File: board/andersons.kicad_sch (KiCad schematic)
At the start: 13 parts, among them J10 768250002, J11 768250002, J12 768250002, J13 768250002, J14 768250002, J15 768250002, J16 768250002, J17 768250002, J18 768250002, J6 768250002, J7 768250002, J8 768250002, J9 768250002

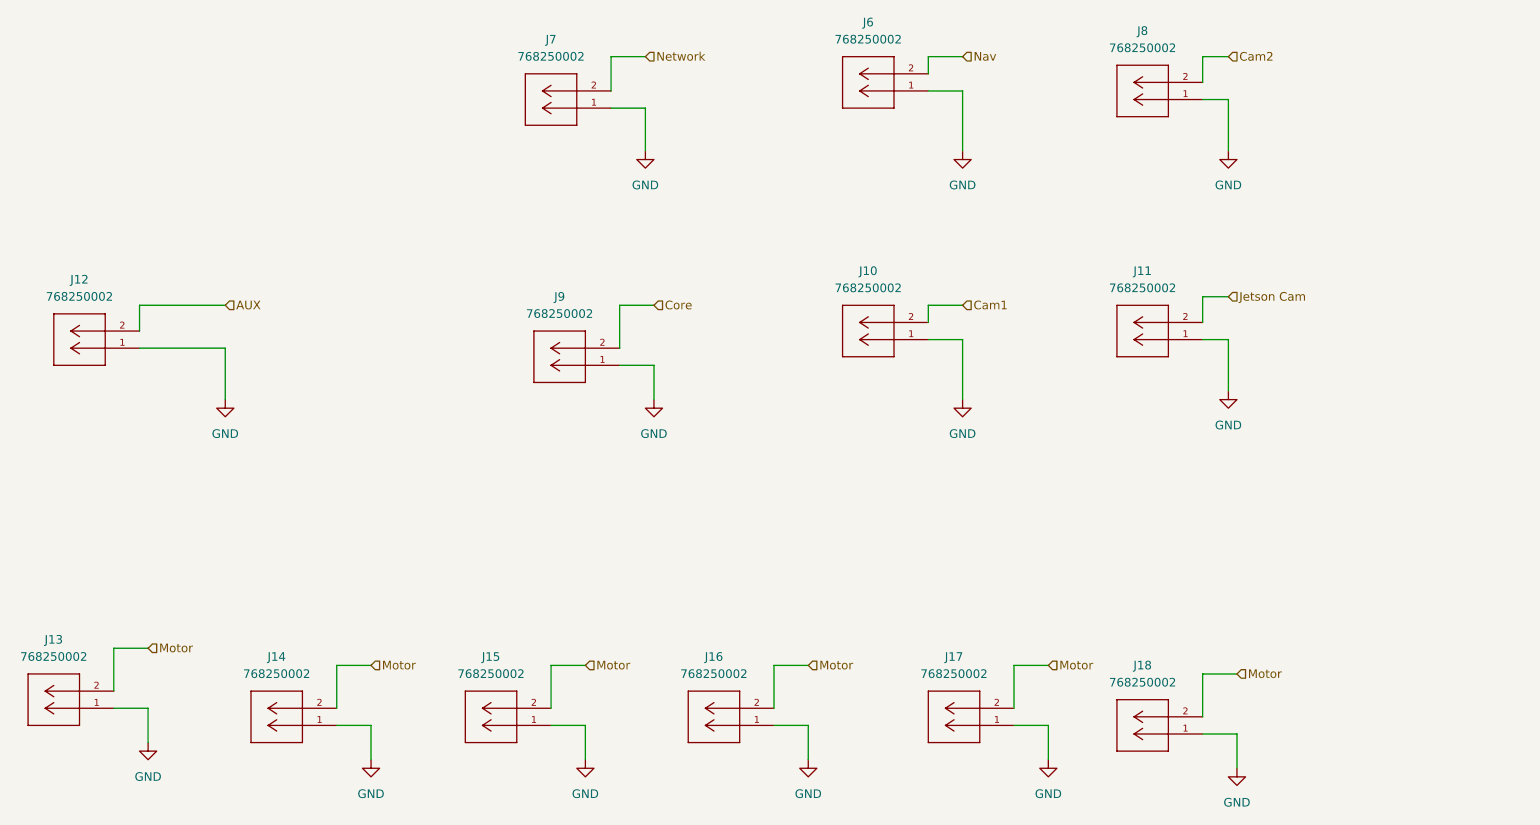
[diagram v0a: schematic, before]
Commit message: Center schematics and layout for prettiness
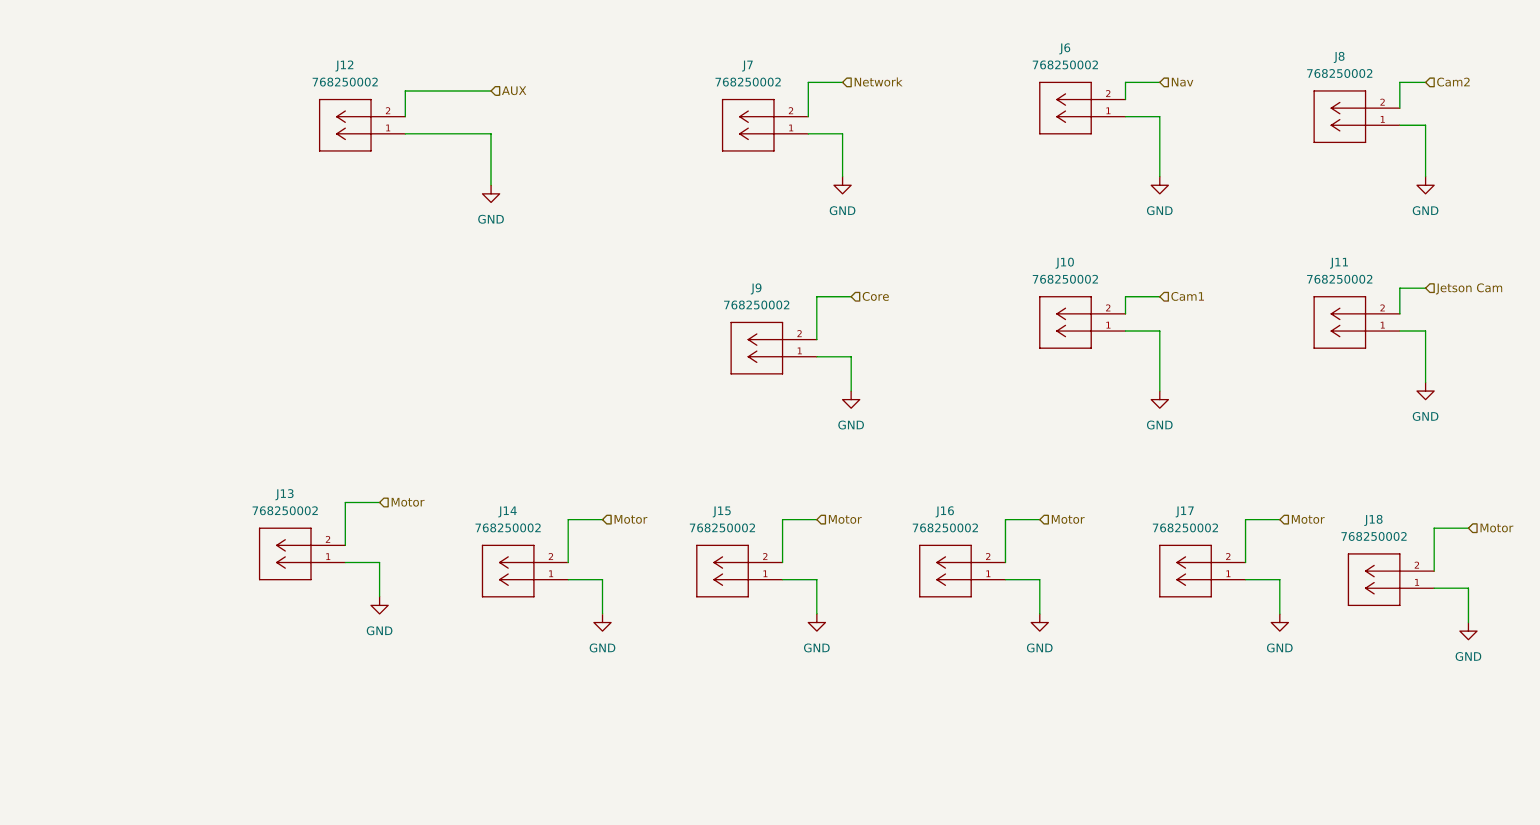
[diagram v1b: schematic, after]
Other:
- moved on the sheet: J10, J11, J12, J13, J14, J15, J16, J17, J18, J6, J7, J8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

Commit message: add label for battery sensing molex connector
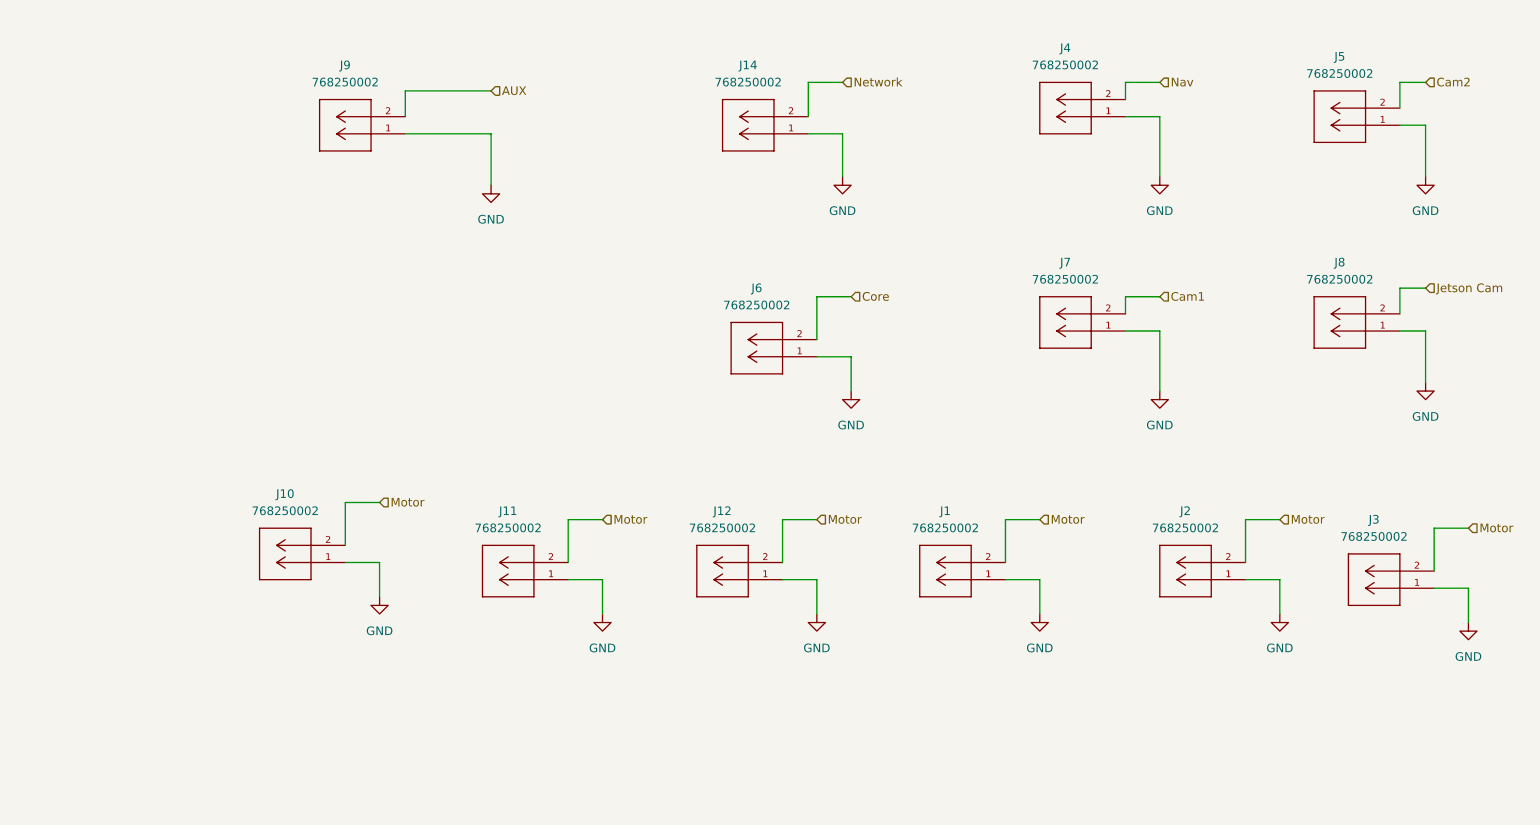
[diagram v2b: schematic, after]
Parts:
- renumbered J16 to J1, J13 to J10, J14 to J11, J15 to J12, J7 to J14, J17 to J2, J18 to J3, J6 to J4, J8 to J5, J9 to J6, J10 to J7, J11 to J8, J12 to J9
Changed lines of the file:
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@@
 		(dnp no)
 		(fields_autoplaced yes)
-		(property "Reference" "J6"
+		(property "Reference" "J4"
 			(at 176.53 39.37 0)
 			(effects
@@
 			(project ""
 				(path "/7eaa639d-7062-45e7-be05-1c2855431307/7df83f93-7851-4dc4-9a38-c4dfcc370e8d"
-					(reference "J6")
+					(reference "J4")
 					(unit 1)
 				)
@@
 		(dnp no)
 		(fields_autoplaced yes)
-		(property "Reference" "J18"
+		(property "Reference" "J3"
 			(at 222.25 109.22 0)
 			(effects
@@
 			(project "PowerManagementBoard"
 				(path "/7eaa639d-7062-45e7-be05-1c2855431307/7df83f93-7851-4dc4-9a38-c4dfcc370e8d"
-					(reference "J18")
+					(reference "J3")
 					(unit 1)
 				)
@@
 		(dnp no)
 		(fields_autoplaced yes)
-		(property "Reference" "J17"
+		(property "Reference" "J2"
 			(at 194.31 107.95 0)
 			(effects
@@
 			(project "PowerManagementBoard"
 				(path "/7eaa639d-7062-45e7-be05-1c2855431307/7df83f93-7851-4dc4-9a38-c4dfcc370e8d"
-					(reference "J17")
+					(reference "J2")
 					(unit 1)
 				)
@@
 		(dnp no)
 		(fields_autoplaced yes)
-		(property "Reference" "J7"
+		(property "Reference" "J14"
 			(at 129.54 41.91 0)
 			(effects
@@
 			(project "PowerManagementBoard"
 				(path "/7eaa639d-7062-45e7-be05-1c2855431307/7df83f93-7851-4dc4-9a38-c4dfcc370e8d"
-					(reference "J7")
+					(reference "J14")
 					(unit 1)
 				)
@@
 		(dnp no)
 		(fields_autoplaced yes)
-		(property "Reference" "J12"
+		(property "Reference" "J9"
 			(at 69.85 41.91 0)
 			(effects
@@
 			(project "PowerManagementBoard"
 				(path "/7eaa639d-7062-45e7-be05-1c2855431307/7df83f93-7851-4dc4-9a38-c4dfcc370e8d"
-					(reference "J12")
+					(reference "J9")
 					(unit 1)
 				)
@@
 		(dnp no)
 		(fields_autoplaced yes)
-		(property "Reference" "J9"
+		(property "Reference" "J6"
 			(at 130.81 74.93 0)
 			(effects
@@
 			(project "PowerManagementBoard"
 				(path "/7eaa639d-7062-45e7-be05-1c2855431307/7df83f93-7851-4dc4-9a38-c4dfcc370e8d"
-					(reference "J9")
+					(reference "J6")
 					(unit 1)
 				)
@@
 		(dnp no)
 		(fields_autoplaced yes)
-		(property "Reference" "J16"
+		(property "Reference" "J1"
 			(at 158.75 107.95 0)
 			(effects
@@
 			(project "PowerManagementBoard"
 				(path "/7eaa639d-7062-45e7-be05-1c2855431307/7df83f93-7851-4dc4-9a38-c4dfcc370e8d"
-					(reference "J16")
+					(reference "J1")
 					(unit 1)
 				)
@@
 		(dnp no)
 		(fields_autoplaced yes)
-		(property "Reference" "J8"
+		(property "Reference" "J5"
 			(at 217.17 40.64 0)
 			(effects
@@
 			(project "PowerManagementBoard"
 				(path "/7eaa639d-7062-45e7-be05-1c2855431307/7df83f93-7851-4dc4-9a38-c4dfcc370e8d"
-					(reference "J8")
+					(reference "J5")
 					(unit 1)
 				)
@@
 		(dnp no)
 		(fields_autoplaced yes)
-		(property "Reference" "J14"
+		(property "Reference" "J11"
 			(at 93.98 107.95 0)
 			(effects
@@
 			(project "PowerManagementBoard"
 				(path "/7eaa639d-7062-45e7-be05-1c2855431307/7df83f93-7851-4dc4-9a38-c4dfcc370e8d"
-					(reference "J14")
+					(reference "J11")
 					(unit 1)
 				)
@@
 		(dnp no)
 		(fields_autoplaced yes)
-		(property "Reference" "J10"
+		(property "Reference" "J7"
 			(at 176.53 71.12 0)
 			(effects
@@
 			(project "PowerManagementBoard"
 				(path "/7eaa639d-7062-45e7-be05-1c2855431307/7df83f93-7851-4dc4-9a38-c4dfcc370e8d"
-					(reference "J10")
+					(reference "J7")
 					(unit 1)
 				)
@@
 		(dnp no)
 		(fields_autoplaced yes)
-		(property "Reference" "J11"
+		(property "Reference" "J8"
 			(at 217.17 71.12 0)
 			(effects
@@
 			(project "PowerManagementBoard"
 				(path "/7eaa639d-7062-45e7-be05-1c2855431307/7df83f93-7851-4dc4-9a38-c4dfcc370e8d"
-					(reference "J11")
+					(reference "J8")
 					(unit 1)
 				)
@@
 		(dnp no)
 		(fields_autoplaced yes)
-		(property "Reference" "J15"
+		(property "Reference" "J12"
 			(at 125.73 107.95 0)
 			(effects
@@
 			(project "PowerManagementBoard"
 				(path "/7eaa639d-7062-45e7-be05-1c2855431307/7df83f93-7851-4dc4-9a38-c4dfcc370e8d"
-					(reference "J15")
+					(reference "J12")
 					(unit 1)
 				)
@@
 		(dnp no)
 		(fields_autoplaced yes)
-		(property "Reference" "J13"
+		(property "Reference" "J10"
 			(at 60.96 105.41 0)
 			(effects
@@
 			(project "PowerManagementBoard"
 				(path "/7eaa639d-7062-45e7-be05-1c2855431307/7df83f93-7851-4dc4-9a38-c4dfcc370e8d"
-					(reference "J13")
-					(unit 1)
-				)
+					(reference "J10")
+					(unit 1)
+				)
